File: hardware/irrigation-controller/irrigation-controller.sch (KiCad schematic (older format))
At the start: 59 parts, among them J1 ATMEGA ICSP, J2 ATMEGA UART, J3 RF Module, K1 UA2-5NU, Q1 MMBT3904, Q2 2N7002, Q3 2N7002, Q4 2N7002, Q5 2N7002, SW1 SPST, U1 AQY280EH, U2 ATmega328P-AU, U3 AQY280EH, U4 TPS54331DR, U5 TPS54331DR, U6 MAX485, Y1 8MHz

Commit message: Add more controller board connectors
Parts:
- added J1: RELAY_1, Connector_JST:JST_XH_B2B-XH-A_1x02_P2.50mm_Vertical, symbol Connector:Conn_01x02_Male
- added J2: RELAY_2, Connector_JST:JST_XH_B2B-XH-A_1x02_P2.50mm_Vertical, symbol Connector:Conn_01x02_Male
- added J6: RELAY_3A, Connector_JST:JST_XH_B3B-XH-A_1x03_P2.50mm_Vertical, symbol Connector:Conn_01x03_Male
- added J7: RELAY_3B, Connector_JST:JST_XH_B3B-XH-A_1x03_P2.50mm_Vertical, symbol Connector:Conn_01x03_Male
- added J?: RS485, Connector_JST:JST_XH_B3B-XH-A_1x03_P2.50mm_Vertical, symbol Connector:Conn_01x03_Male
- added J?: I2C, Connector_JST:JST_XH_B4B-XH-A_1x04_P2.50mm_Vertical, symbol Connector:Conn_01x04_Male
- added J?: IO, Connector_PinHeader_2.54mm:PinHeader_2x04_P2.54mm_Vertical, symbol Connector:Conn_01x08_Male
- added U?: ESP32-WROOM-32E, RF_Module:ESP32-WROOM-32, symbol RF_Module:ESP32-WROOM-32
- C1, C10, C11, C12, C13, C14, C15, C16, C17, C18, C2, C3, C4, C5, C6, C7, C8, C9, D1, D2, D3, Q1, Q2, Q3, Q4, Q5, R1, R10, R11, R12, R13, R14, R15, R16, R17, R18, R19, R2, R3, R4, R5, R6, R7, R8, R9, U2, U4, U5, Y1: Purchase Link (none) -> NA
- renumbered J1 to J3, J2 to J4, J3 to J5
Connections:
- wire segments 222 -> 236
- no-connect marks 18 -> 4
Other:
- note added: "Todo:\nESP32\nExtra signal relay?"
- note removed: "TODO:\nRelay connectors\nRS-485 connector\nIO expansion connectors"
- note removed: "Todo:\nExtra IO: i2c, spi, io pins\nESP32\nExtra signal relay?"
- moved on the sheet: D1, J3, J4, J5, K1, Q1, R1

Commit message: Add controller relay 4
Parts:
- removed U?: ESP32-WROOM-32E, RF_Module:ESP32-WROOM-32, symbol RF_Module:ESP32-WROOM-32
- added D?: SM4007PL, Diode_SMD:D_SMA, symbol Device:D
- added J?: RELAY_4A, Connector_JST:JST_XH_B3B-XH-A_1x03_P2.50mm_Vertical, symbol Connector:Conn_01x03_Male
- added J?: RELAY_4B, Connector_JST:JST_XH_B3B-XH-A_1x03_P2.50mm_Vertical, symbol Connector:Conn_01x03_Male
- added K?: UA2-5NU, kicad-lib-jlcpcb:Relay_DPDT_NEXEM_UA2_Pitch3.2mm, symbol Relay:EC2-5NU
- added Q?: MMBT3904, Package_TO_SOT_SMD:SOT-23, symbol Transistor_BJT:MMBT3904
- added R?: 2.2k, Resistor_SMD:R_0402_1005Metric, symbol Device:R
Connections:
- net labels added: R4AC, R4ANC, R4ANO, R4BC, R4BNC, R4BNO
- wire segments 236 -> 262
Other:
- note added: "Note: A04 shared with RELAY4"
- moved on the sheet: D1, J1, J2, J3, J4, J5, J6, J7, J?, K1, Q1, Q2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

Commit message: Add i2c_2
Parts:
- added J9: I2C_2, Connector_JST:JST_XH_B4B-XH-A_1x04_P2.50mm_Vertical, symbol Connector:Conn_01x04_Male
- J10: renamed from J?; Purchase Link (none) -> https://au.element14.com/amphenol-icc/77313-801-20lf/conn-h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
- J2: renamed from J?; value I2C -> I2C_1
- J3, J4: Purchase Link (none) -> https://au.element14.com/amphenol-icc/77313-801-20lf/conn-h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
- J5: Purchase Link (none) -> https://au.element14.com/amphenol-icc/10129378-920003blf/co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
- gave numbers to parts that had none: 7
- renumbered D2 to D3, D3 to D4, J2 to J11, J7 to J12, J1 to J6, J6 to J7, Q2 to Q3, Q3 to Q4, Q4 to Q5, Q5 to Q6, R7 to R10, R10 to R11, R11 to R13, R13 to R14, R14 to R15, R15 to R16, R16 to R17, R17 to R18, R18 to R19, R19 to R20, R4 to R5, R5 to R6, R6 to R7
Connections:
- net +3V3: now also J9.4 (Pin_4)
- net ASCL: now also J9.2 (Pin_2)
- net ASDA: now also J9.3 (Pin_3)
- net GND: now also J9.1 (Pin_1)
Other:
- note added: "Note: AI04 shared with RELAY_4"
- note removed: "Note: A04 shared with RELAY4"
- note removed: "Todo:\nESP32\nExtra signal relay?"
- moved on the sheet: J1, J10, J2

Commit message: Add controller PWR input
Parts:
- added J6: PWR, Connector_JST:JST_XH_B2B-XH-A_1x02_P2.50mm_Vertical, symbol Connector:Conn_01x02_Male
- renumbered J9 to J10, J10 to J11, J11 to J12, J12 to J13, J13 to J14, J6 to J7, J7 to J8, J8 to J9
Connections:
- net +24V: now also J6.1 (Pin_1)
- net GND: now also J6.2 (Pin_2)
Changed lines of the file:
@@
 NoConn ~ 1050 2150
 $Comp
-L Connector:Conn_01x02_Male J6
+L Connector:Conn_01x02_Male J7
 U 1 1 613ABED8
 P 10300 900
-F 0 "J6" V 10135 878 50  0000 C CNN
+F 0 "J7" V 10135 878 50  0000 C CNN
 F 1 "RELAY_1" V 10226 878 50  0000 C CNN
 F 2 "Connector_JST:JST_XH_B2B-XH-A_1x02_P2.50mm_Vertical" H 10300 900 50  0001 C CNN
@@
 $EndComp
 $Comp
-L Connector:Conn_01x02_Male J11
+L Connector:Conn_01x02_Male J12
 U 1 1 613DF424
 P 10700 900
-F 0 "J11" V 10535 878 50  0000 C CNN
+F 0 "J12" V 10535 878 50  0000 C CNN
 F 1 "RELAY_2" V 10626 878 50  0000 C CNN
 F 2 "Connector_JST:JST_XH_B2B-XH-A_1x02_P2.50mm_Vertical" H 10700 900 50  0001 C CNN
@@
 $EndComp
 $Comp
-L Connector:Conn_01x03_Male J7
+L Connector:Conn_01x03_Male J8
 U 1 1 613F8F16
 P 10300 1750
-F 0 "J7" V 10135 1728 50  0000 C CNN
+F 0 "J8" V 10135 1728 50  0000 C CNN
 F 1 "RELAY_3A" V 10226 1728 50  0000 C CNN
 F 2 "Connector_JST:JST_XH_B3B-XH-A_1x03_P2.50mm_Vertical" H 10300 1750 50  0001 C CNN
@@
 $EndComp
 $Comp
-L Connector:Conn_01x03_Male J12
+L Connector:Conn_01x03_Male J13
 U 1 1 6142E79F
 P 10750 1750
-F 0 "J12" V 10585 1728 50  0000 C CNN
+F 0 "J13" V 10585 1728 50  0000 C CNN
 F 1 "RELAY_3B" V 10676 1728 50  0000 C CNN
 F 2 "Connector_JST:JST_XH_B3B-XH-A_1x03_P2.50mm_Vertical" H 10750 1750 50  0001 C CNN
@@
 RFSET
 $Comp
-L power:GND #PWR037
+L power:GND #PWR038
 U 1 1 614A1B8E
 P 9800 2050
-F 0 "#PWR037" H 9800 1800 50  0001 C CNN
+F 0 "#PWR038" H 9800 1800 50  0001 C CNN
 F 1 "GND" H 9805 1877 50  0000 C CNN
 F 2 "" H 9800 2050 50  0001 C CNN
@@
 $EndComp
 $Comp
-L power:GND #PWR036
+L power:GND #PWR037
 U 1 1 614A3FA6
 P 9800 1300
-F 0 "#PWR036" H 9800 1050 50  0001 C CNN
+F 0 "#PWR037" H 9800 1050 50  0001 C CNN
 F 1 "GND" H 9805 1127 50  0000 C CNN
 F 2 "" H 9800 1300 50  0001 C CNN
@@
 	9150 4850 9150 4750
 $Comp
-L power:GND #PWR035
+L power:GND #PWR036
 U 1 1 6154C177
 P 9500 4850
-F 0 "#PWR035" H 9500 4600 50  0001 C CNN
+F 0 "#PWR036" H 9500 4600 50  0001 C CNN
 F 1 "GND" H 9505 4677 50  0000 C CNN
 F 2 "" H 9500 4850 50  0001 C CNN
@@
 	9500 4800 9500 4850
 $Comp
-L power:+3.3V #PWR039
+L power:+3.3V #PWR040
 U 1 1 6161AE6C
 P 9900 3800
-F 0 "#PWR039" H 9900 3650 50  0001 C CNN
+F 0 "#PWR040" H 9900 3650 50  0001 C CNN
 F 1 "+3.3V" H 9915 3973 50  0000 C CNN
 F 2 "" H 9900 3800 50  0001 C CNN
@@
 	10100 3900 10100 3800
 $Comp
-L power:GND #PWR042
+L power:GND #PWR044
 U 1 1 61629A77
 P 10850 3900
-F 0 "#PWR042" H 10850 3650 50  0001 C CNN
+F 0 "#PWR044" H 10850 3650 50  0001 C CNN
 F 1 "GND" H 10855 3727 50  0000 C CNN
 F 2 "" H 10850 3900 50  0001 C CNN
@@
 AIO5
 $Comp
-L Connector:Conn_01x08_Male J10
+L Connector:Conn_01x08_Male J11
 U 1 1 61618367
 P 10500 3600
-F 0 "J10" V 10300 3500 50  0000 L CNN
+F 0 "J11" V 10300 3500 50  0000 L CNN
 F 1 "IO" V 10400 3300 50  0000 L CNN
 F 2 "Connector_PinHeader_2.54mm:PinHeader_2x04_P2.54mm_Vertical" H 10500 3600 50  0001 C CNN
@@
 	9800 2850 9800 2950
 $Comp
-L power:GND #PWR038
+L power:GND #PWR039
 U 1 1 61384F23
 P 9800 2950
-F 0 "#PWR038" H 9800 2700 50  0001 C CNN
+F 0 "#PWR039" H 9800 2700 50  0001 C CNN
 F 1 "GND" H 9805 2777 50  0000 C CNN
 F 2 "" H 9800 2950 50  0001 C CNN
@@
 R4BNC
 $Comp
-L Connector:Conn_01x03_Male J8
+L Connector:Conn_01x03_Male J9
 U 1 1 6170C91D
 P 10300 2550
-F 0 "J8" V 10135 2528 50  0000 C CNN
+F 0 "J9" V 10135 2528 50  0000 C CNN
 F 1 "RELAY_4A" V 10226 2528 50  0000 C CNN
 F 2 "Connector_JST:JST_XH_B3B-XH-A_1x03_P2.50mm_Vertical" H 10300 2550 50  0001 C CNN
@@
 $EndComp
 $Comp
-L Connector:Conn_01x03_Male J13
+L Connector:Conn_01x03_Male J14
 U 1 1 6170C928
 P 10750 2550
-F 0 "J13" V 10585 2528 50  0000 C CNN
+F 0 "J14" V 10585 2528 50  0000 C CNN
 F 1 "RELAY_4B" V 10676 2528 50  0000 C CNN
 F 2 "Connector_JST:JST_XH_B3B-XH-A_1x03_P2.50mm_Vertical" H 10750 2550 50  0001 C CNN
@@
 ASCL
 $Comp
-L Connector:Conn_01x04_Male J9
+L Connector:Conn_01x04_Male J10
 U 1 1 618BA1F4
 P 10400 4550
-F 0 "J9" V 10235 4528 50  0000 C CNN
+F 0 "J10" V 10235 4528 50  0000 C CNN
 F 1 "I2C_2" V 10326 4528 50  0000 C CNN
 F 2 "Connector_JST:JST_XH_B4B-XH-A_1x04_P2.50mm_Vertical" H 10400 4550 50  0001 C CNN
@@
 $EndComp
 $Comp
-L power:+3.3V #PWR040
+L power:+3.3V #PWR042
 U 1 1 618BA1FE
 P 10000 4750
-F 0 "#PWR040" H 10000 4600 50  0001 C CNN
+F 0 "#PWR042" H 10000 4600 50  0001 C CNN
 F 1 "+3.3V" H 10015 4923 50  0000 C CNN
 F 2 "" H 10000 4750 50  0001 C CNN
@@
 	10200 4850 10200 4750
 $Comp
-L power:GND #PWR041
+L power:GND #PWR043
 U 1 1 618BA20B
 P 10550 4850
-F 0 "#PWR041" H 10550 4600 50  0001 C CNN
+F 0 "#PWR043" H 10550 4600 50  0001 C CNN
 F 1 "GND" H 10555 4677 50  0000 C CNN
 F 2 "" H 10550 4850 50  0001 C CNN
@@
 Wire Notes Line
 	8650 600  8650 6450
+$Comp
+L power:PWR_FLAG #FLG04
+U 1 1 61923EF8
+P 9950 5700
+F 0 "#FLG04" H 9950 5775 50  0001 C CNN
+F 1 "PWR_FLAG" H 9950 5873 50  0000 C CNN
+F 2 "" H 9950 5700 50  0001 C CNN
+F 3 "~" H 9950 5700 50  0001 C CNN
+	1    9950 5700
+	-1   0    0    1
+$EndComp
+$Comp
+L power:+24V #PWR041
+U 1 1 61924F74
+P 9950 5600
+F 0 "#PWR041" H 9950 5450 50  0001 C CNN
+F 1 "+24V" H 9965 5773 50  0000 C CNN
+F 2 "" H 9950 5600 50  0001 C CNN
+F 3 "" H 9950 5600 50  0001 C CNN
+	1    9950 5600
+	1    0    0    -1
+$EndComp
+$Comp
+L Connector:Conn_01x02_Male J6
+U 1 1 61926C7F
+P 9750 5400
+F 0 "J6" V 9585 5378 50  0000 C CNN
+F 1 "PWR" V 9676 5378 50  0000 C CNN
+F 2 "Connector_JST:JST_XH_B2B-XH-A_1x02_P2.50mm_Vertical" H 9750 5400 50  0001 C CNN
+F 3 "~" H 9750 5400 50  0001 C CNN
+F 4 "https://au.mouser.com/ProductDetail/426-FIT0255" V 9750 5400 50  0001 C CNN "Purchase Link"
+	1    9750 5400
+	0    1    1    0
+$EndComp
+Wire Wire Line
+	9750 5600 9750 5700
+Wire Wire Line
+	9750 5700 9950 5700
+Wire Wire Line
+	9950 5700 9950 5600
+Connection ~ 9950 5700
+$Comp
+L power:GND #PWR035
+U 1 1 61962CBA
+P 9400 5700
+F 0 "#PWR035" H 9400 5450 50  0001 C CNN
+F 1 "GND" H 9405 5527 50  0000 C CNN
+F 2 "" H 9400 5700 50  0001 C CNN
+F 3 "" H 9400 5700 50  0001 C CNN
+	1    9400 5700
+	1    0    0    -1
+$EndComp
+$Comp
+L power:PWR_FLAG #FLG03
+U 1 1 619D5328
+P 9400 5600
+F 0 "#FLG03" H 9400 5675 50  0001 C CNN
+F 1 "PWR_FLAG" H 9400 5773 50  0000 C CNN
+F 2 "" H 9400 5600 50  0001 C CNN
+F 3 "~" H 9400 5600 50  0001 C CNN
+	1    9400 5600
+	1    0    0    -1
+$EndComp
+Wire Wire Line
+	9400 5600 9400 5700
+Wire Wire Line
+	9650 5600 9650 5700
+Wire Wire Line
+	9650 5700 9400 5700
+Connection ~ 9400 5700
+$Comp
+L power:PWR_FLAG #FLG01
+U 1 1 619FC90F
+P 6850 850
+F 0 "#FLG01" H 6850 925 50  0001 C CNN
+F 1 "PWR_FLAG" H 6850 1023 50  0000 C CNN
+F 2 "" H 6850 850 50  0001 C CNN
+F 3 "~" H 6850 850 50  0001 C CNN
+	1    6850 850
+	1    0    0    -1
+$EndComp
+Wire Wire Line
+	6850 950  6850 850
+$Comp
+L power:PWR_FLAG #FLG02
+U 1 1 61A113AC
+P 6850 3050
+F 0 "#FLG02" H 6850 3125 50  0001 C CNN
+F 1 "PWR_FLAG" H 6850 3223 50  0000 C CNN
+F 2 "" H 6850 3050 50  0001 C CNN
+F 3 "~" H 6850 3050 50  0001 C CNN
+	1    6850 3050
+	1    0    0    -1
+$EndComp
+Wire Wire Line
+	6850 3050 6850 3150
+$Comp
+L power:PWR_FLAG #FLG0101
+U 1 1 61A89071
+P 7900 3050
+F 0 "#FLG0101" H 7900 3125 50  0001 C CNN
+F 1 "PWR_FLAG" H 7900 3223 50  0000 C CNN
+F 2 "" H 7900 3050 50  0001 C CNN
+F 3 "~" H 7900 3050 50  0001 C CNN
+	1    7900 3050
+	1    0    0    -1
+$EndComp
+Wire Wire Line
+	7900 3050 7900 3150
+$Comp
+L power:PWR_FLAG #FLG0102
+U 1 1 61A9CB97
+P 7900 850
+F 0 "#FLG0102" H 7900 925 50  0001 C CNN
+F 1 "PWR_FLAG" H 7900 1023 50  0000 C CNN
+F 2 "" H 7900 850 50  0001 C CNN
+F 3 "~" H 7900 850 50  0001 C CNN
+	1    7900 850
+	1    0    0    -1
+$EndComp
+Wire Wire Line
+	7900 850  7900 950
 $EndSCHEMATC

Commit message: Add custom library
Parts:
- K1, K2: footprint kicad-lib-jlcpcb:Relay_DPDT_NEXEM_UA2_Pitch3.2mm -> lib:Relay_DPDT_NEXEM_UA2_Pitch3.2mm
- SW1: footprint kicad-lib-jlcpcb:SW_SPST_THT_5.0mm -> lib:SW_SPST_THT_5.0mm
- U4, U5: footprint TPS54331DDAR:Texas_Instruments-TPS54331DR-Level_A -> TPS54331DR:Texas_Instruments-TPS54331DR-Level_A; symbol IC_TI_TPS54331DR:TPS54331DR -> TPS54331DR:TPS54331DR
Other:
- note added: "RS-485 Termination"
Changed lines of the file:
@@
 F 0 "SW1" V 2904 3898 50  0000 L CNN
 F 1 "SPST" V 2995 3898 50  0000 L CNN
-F 2 "kicad-lib-jlcpcb:SW_SPST_THT_5.0mm" H 2950 3800 50  0001 C CNN
+F 2 "lib:SW_SPST_THT_5.0mm" H 2950 3800 50  0001 C CNN
 F 3 "https://www.farnell.com/datasheets/3176355.pdf" H 2950 3800 50  0001 C CNN
 F 4 "" H 2950 3800 50  0001 C CNN "Purchase link"
@@
 F 0 "K1" V 1133 7100 50  0000 C CNN
 F 1 "UA2-5NU" V 1224 7100 50  0000 C CNN
-F 2 "kicad-lib-jlcpcb:Relay_DPDT_NEXEM_UA2_Pitch3.2mm" H 1900 7100 50  0001 C CNN
+F 2 "lib:Relay_DPDT_NEXEM_UA2_Pitch3.2mm" H 1900 7100 50  0001 C CNN
 F 3 "https://www.farnell.com/datasheets/2302216.pdf" H 1900 7100 50  0001 C CNN
 F 4 "https://au.element14.com/nexem/ua2-5nu/signal-relay-dpdt-1a-250vac-th/dp/2766147" H 1900 7100 50  0001 C CNN "Purchase Link"
@@
 RS485A
 $Comp
-L IC_TI_TPS54331DR:TPS54331DR U4
+L TPS54331DR:TPS54331DR U4
 U 1 1 6138537B
 P 5250 950
 F 0 "U4" H 5850 1215 50  0000 C CNN
 F 1 "TPS54331DR" H 5850 1124 50  0000 C CNN
-F 2 "TPS54331DDAR:Texas_Instruments-TPS54331DR-Level_A" H 6150 600 50  0001 C CNN
+F 2 "TPS54331DR:Texas_Instruments-TPS54331DR-Level_A" H 6150 600 50  0001 C CNN
 F 3 "https://www.ti.com/lit/ds/symlink/tps54331.pdf" H 6250 500 50  0001 C CNN
 F 4 "C9865" H 5250 950 50  0001 C CNN "JLCPCB Part"
@@
 3.47v
 $Comp
-L IC_TI_TPS54331DR:TPS54331DR U5
+L TPS54331DR:TPS54331DR U5
 U 1 1 615282A6
 P 5250 3150
 F 0 "U5" H 5850 3415 50  0000 C CNN
 F 1 "TPS54331DR" H 5850 3324 50  0000 C CNN
-F 2 "TPS54331DDAR:Texas_Instruments-TPS54331DR-Level_A" H 6150 2800 50  0001 C CNN
+F 2 "TPS54331DR:Texas_Instruments-TPS54331DR-Level_A" H 6150 2800 50  0001 C CNN
 F 3 "https://www.ti.com/lit/ds/symlink/tps54331.pdf" H 6250 2700 50  0001 C CNN
 F 4 "C9865" H 5250 3150 50  0001 C CNN "JLCPCB Part"
@@
 L power:+5V #PWR021
 U 1 1 6162E314
-P 6000 6250
-F 0 "#PWR021" H 6000 6100 50  0001 C CNN
-F 1 "+5V" H 6015 6423 50  0000 C CNN
-F 2 "" H 6000 6250 50  0001 C CNN
-F 3 "" H 6000 6250 50  0001 C CNN
-	1    6000 6250
-	1    0    0    -1
-$EndComp
-Wire Wire Line
-	6000 6250 6000 6350
+P 6000 6350
+F 0 "#PWR021" H 6000 6200 50  0001 C CNN
+F 1 "+5V" H 6015 6523 50  0000 C CNN
+F 2 "" H 6000 6350 50  0001 C CNN
+F 3 "" H 6000 6350 50  0001 C CNN
+	1    6000 6350
+	1    0    0    -1
+$EndComp
 $Comp
 L power:GND #PWR019
@@
 Connection ~ 6000 5600
 Wire Wire Line
-	7200 5600 7200 5950
-Wire Wire Line
-	7200 5950 5800 5950
-Wire Wire Line
-	5800 5950 5800 6000
+	7200 5600 7200 6000
 Connection ~ 7200 5600
 Wire Wire Line
-	8350 5600 8350 6000
-Wire Wire Line
-	8350 6000 5900 6000
-Wire Wire Line
-	5900 6000 5900 6100
-Wire Wire Line
-	5900 6100 5250 6100
+	8350 5600 8350 6100
 Connection ~ 8350 5600
 Wire Wire Line
@@
 Wire Wire Line
 	5150 6850 5300 6850
-Wire Wire Line
-	5150 6000 5800 6000
 Wire Wire Line
 	5050 6950 5300 6950
@@
 F 0 "K2" V 3233 7100 50  0000 C CNN
 F 1 "UA2-5NU" V 3324 7100 50  0000 C CNN
-F 2 "kicad-lib-jlcpcb:Relay_DPDT_NEXEM_UA2_Pitch3.2mm" H 4000 7100 50  0001 C CNN
+F 2 "lib:Relay_DPDT_NEXEM_UA2_Pitch3.2mm" H 4000 7100 50  0001 C CNN
 F 3 "https://www.farnell.com/datasheets/2302216.pdf" H 4000 7100 50  0001 C CNN
 F 4 "https://au.element14.com/nexem/ua2-5nu/signal-relay-dpdt-1a-250vac-th/dp/2766147" H 4000 7100 50  0001 C CNN "Purchase Link"
@@
 Wire Wire Line
 	7900 850  7900 950
+Wire Wire Line
+	5150 6000 7200 6000
+Wire Wire Line
+	5250 6100 8350 6100
+Text Notes 6100 7200 0    50   ~ 0
+RS-485 Termination
 $EndSCHEMATC

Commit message: Fix relay symbol pins
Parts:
- K1, K2: symbol Relay:EC2-5NU -> lib:UA2-5NU
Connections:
- net R3AC: now also K1.3; no longer K1.4
- net R3ANC: now also K1.2; no longer K1.3
- net R3ANO: now also K1.4; no longer K1.5
- net R3BC: now also K1.6; no longer K1.9
- net R3BNC: now also K1.7; no longer K1.10
- net R3BNO: now also K1.5; no longer K1.8
- net R4AC: now also K2.3; no longer K2.4
- net R4ANC: now also K2.2; no longer K2.3
- net R4ANO: now also K2.4; no longer K2.5
- net R4BC: now also K2.6; no longer K2.9
- net R4BNC: now also K2.7; no longer K2.10
- net R4BNO: now also K2.5; no longer K2.8
- net at D1.2 (A), Q1.3 (C): now also K1.8; no longer K1.12
- net at D2.2 (A), Q2.3 (C): now also K2.8; no longer K2.12
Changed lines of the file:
@@
 AIO2
 $Comp
-L Relay:EC2-5NU K1
+L lib:UA2-5NU K1
 U 1 1 6152BDC7
 P 1900 7100
@@
 	1500 6300 1500 6250
 $Comp
-L Relay:EC2-5NU K2
+L lib:UA2-5NU K2
 U 1 1 615A0129
 P 4000 7100

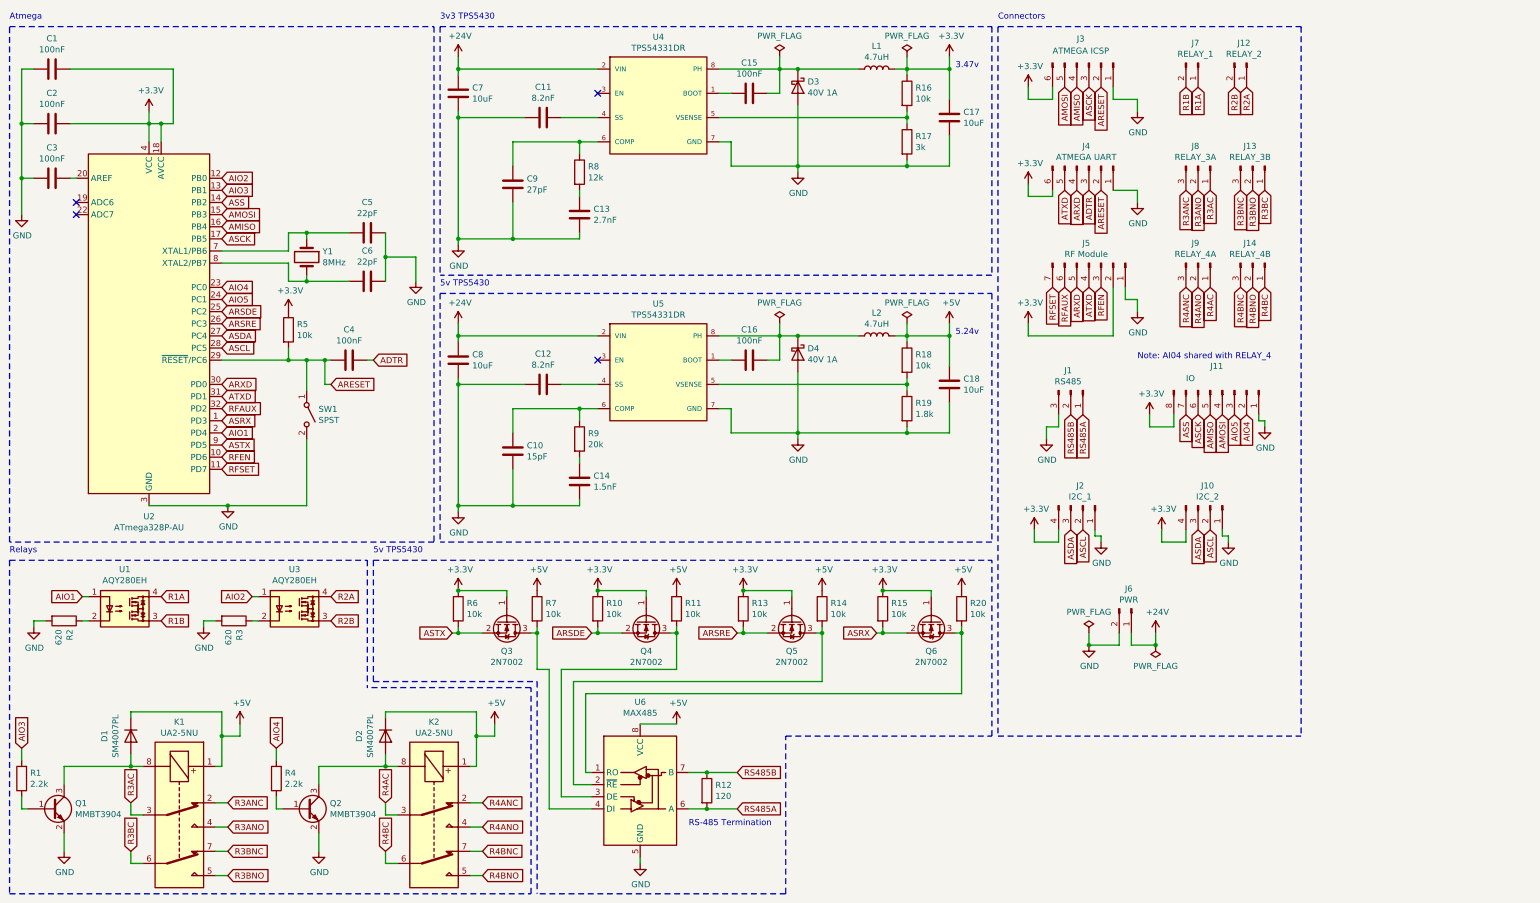
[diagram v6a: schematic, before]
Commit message: Initial controller pcb footprint import
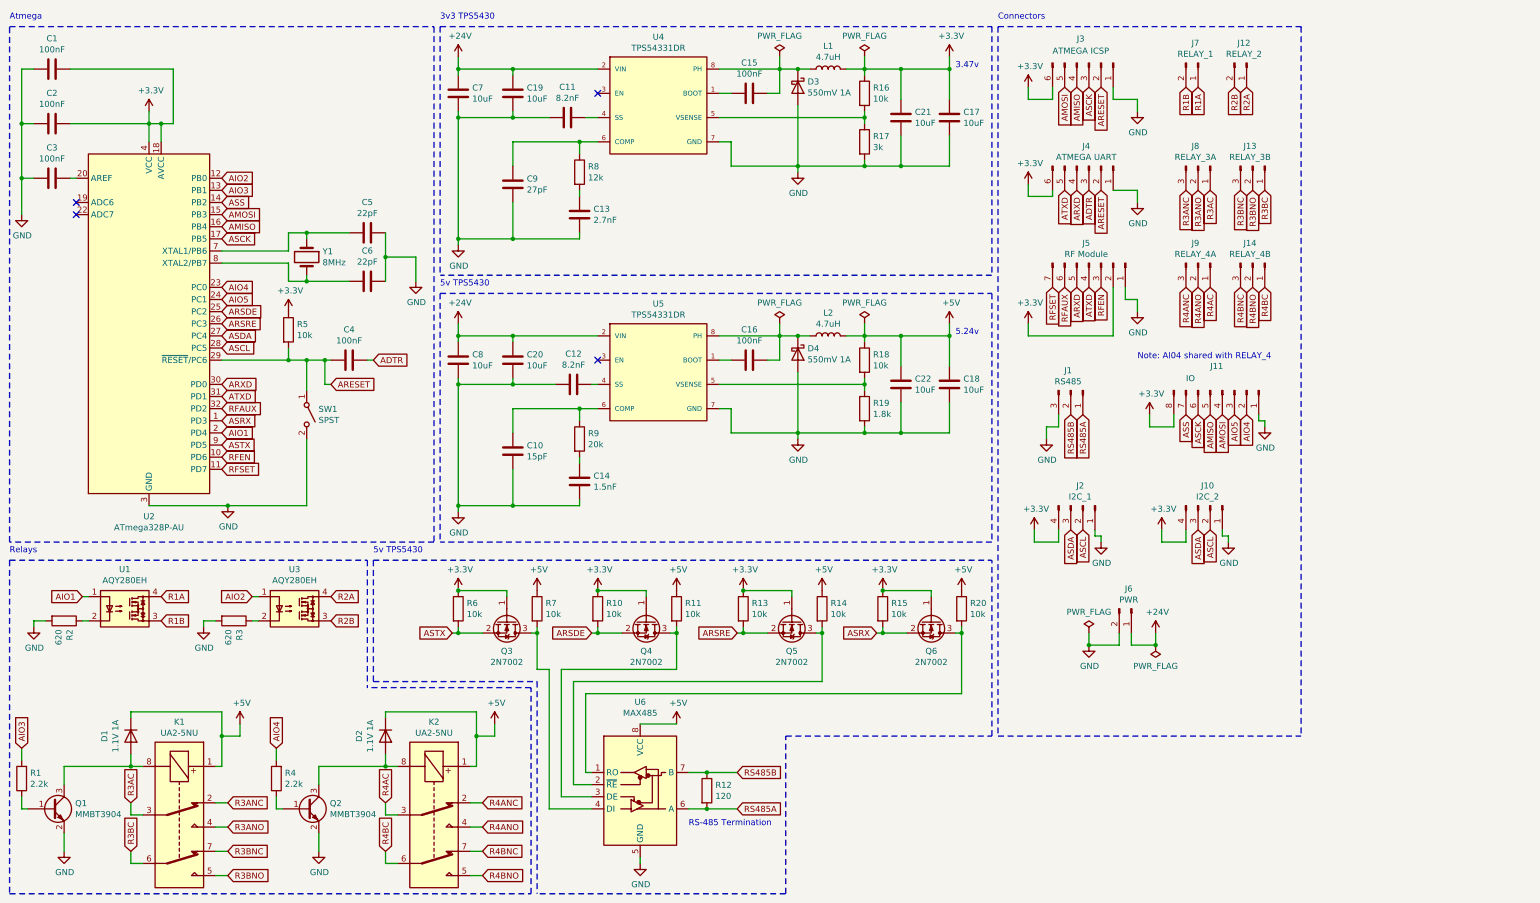
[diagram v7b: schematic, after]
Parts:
- added C19, C20, C21, C22: 10uF, Capacitor_SMD:C_1206_3216Metric, symbol Device:C
- D1, D2: value SM4007PL -> 1.1V 1A
- D3, D4: value 40V 1A -> 550mV 1A
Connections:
- net +24V: now also C19.1, C20.1
- net +3V3: now also C21.1
- net +5V: now also C22.1
- net GND: now also C19.2, C20.2, C21.2, C22.2
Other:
- moved on the sheet: C11, C12, L1, L2, R16, R17, R18, R19
